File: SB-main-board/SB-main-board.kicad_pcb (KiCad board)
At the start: 4 copper layers, 53 x 40 mm, 94 parts, among them J1 XT30PB_IN, J2 USB_C_Receptacle_USB2.0_16P, J3 Excluder, J4 PT100, J5 Hotend, J6 FAN2, J7 LDC, J8 FS, J9 FAN, Q1 BUK9M8R5-40EX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

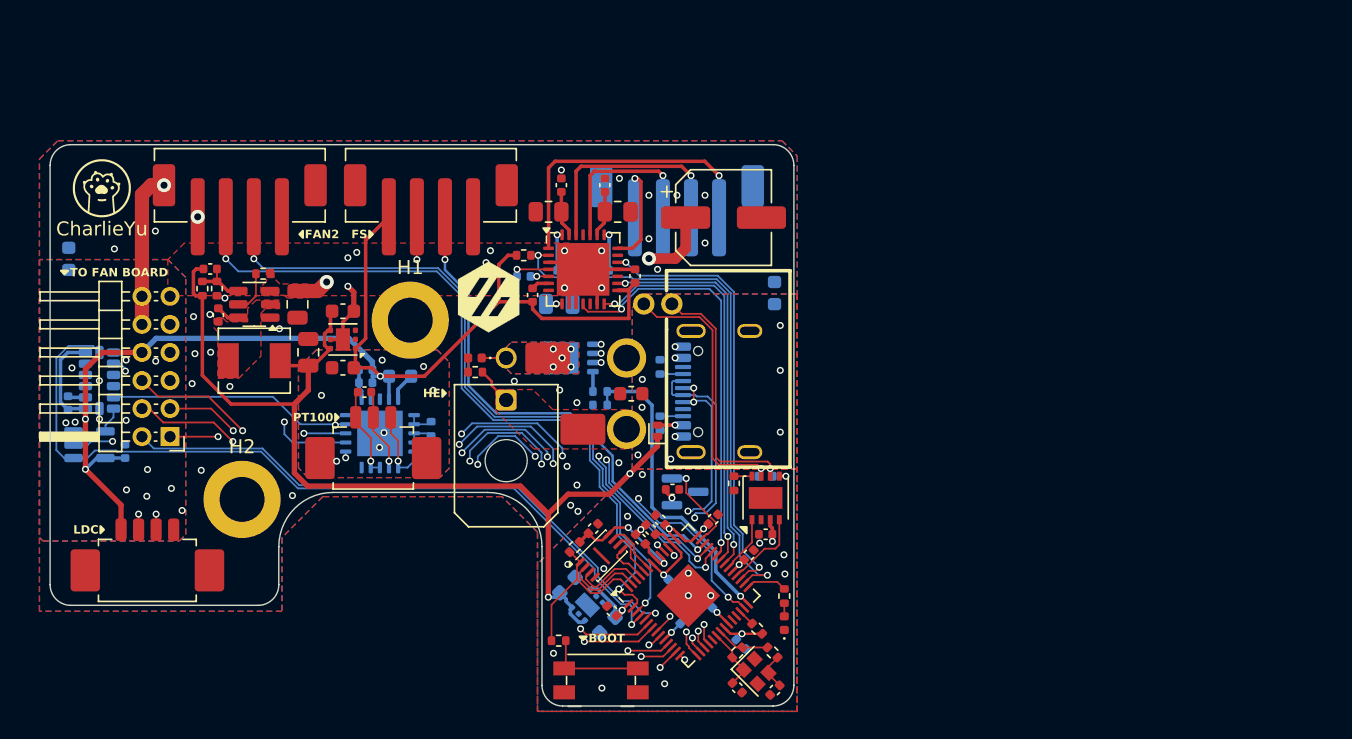
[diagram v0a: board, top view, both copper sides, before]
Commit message: mechanical: fix interference
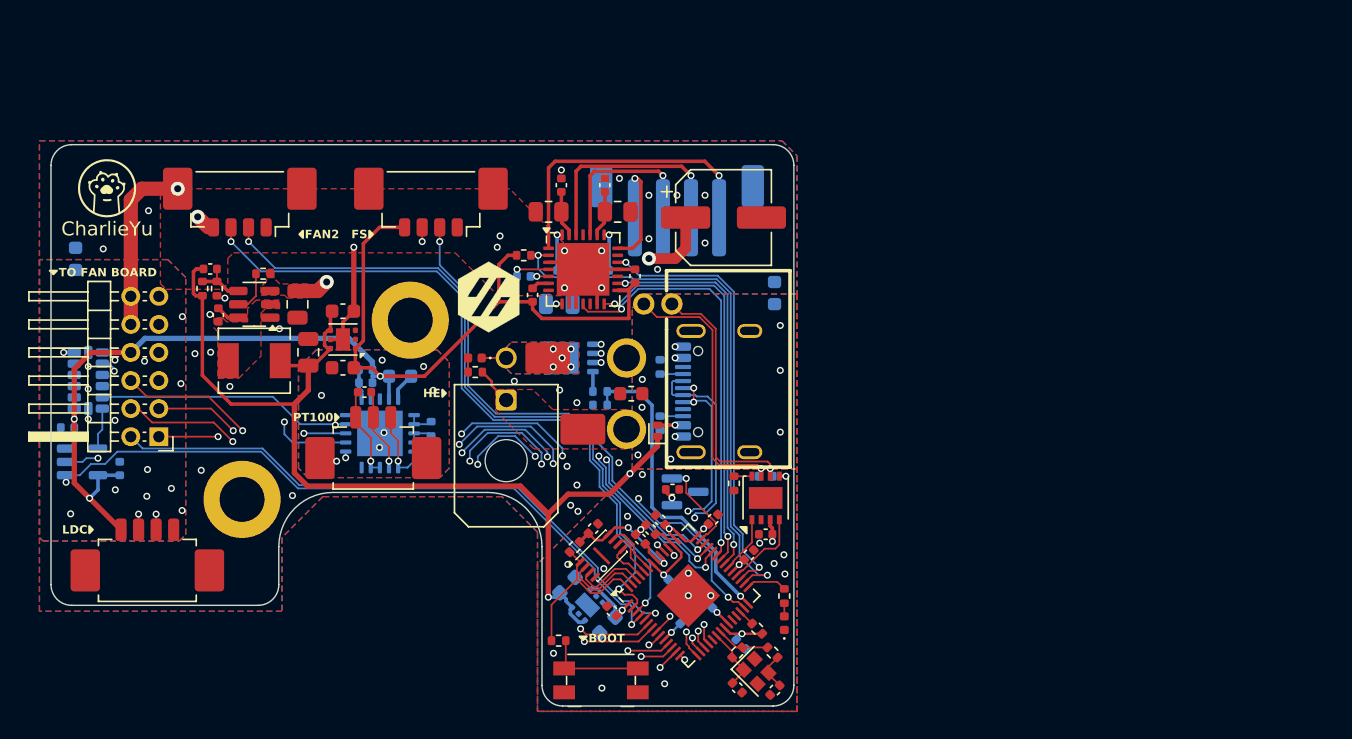
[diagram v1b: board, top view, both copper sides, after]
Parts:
- J6, J8: footprint Library:JST_PH_B4B-PH-SM4-TB_1x04-1MP_P2.00mm_Vertical -> Connector_Molex:Molex_PicoBlade_53398-0471_1x04-1MP_P1.25mm_Vertical
- moved C29 1.75 mm to (80.9, 113.8), turned to 180 degrees
- moved U7 1.34 mm to (81.9, 116.3)
- moved C30 1.28 mm to (84.6, 116.7)
- moved J9 0.80 mm to (87.4, 114.5)
- moved U8 0.80 mm to (82.3, 110.5)
- moved FB3 0.48 mm to (81.4, 101.8)
- moved RFF** 0.37 mm to (83.7, 96.8)
- turned J6 to 180 degrees
- turned J8 to 180 degrees
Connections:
- J6 pad 1: +24V -> GND
- J6 pad 2: /FAN2_PWM -> /FAN2_DET
- J6 pad 3: /FAN2_DET -> /FAN2_PWM
- J6 pad 4: GND -> +24V
- J8 pad 1: +3V3B -> GND
- J8 pad 2: /ENDSTOP0 -> /FS
- J8 pad 3: /FS -> /ENDSTOP0
- J8 pad 4: GND -> +3V3B
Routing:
- net +24V: track 72.3 -> 75.5 mm
- net /SPI0_MOSI: track 58.1 -> 59.7 mm
- net +3V3B: track 92.9 -> 94.4 mm, vias 3 -> 4
- net /FAN2_PWM: track 52.8 -> 51.3 mm
- net PGND: track 11.1 -> 12.6 mm
- net GND: track 25.3 -> 26.7 mm, vias 51 -> 47
- net Net-(U8-SDA/SDI/SDIO): track 1.86 -> 2.98 mm
- net /FAN2_DET: track 50.6 -> 49.5 mm
- net /ENDSTOP0: track 42.1 -> 41.2 mm
- net /SPI0_MISO: track 53.8 -> 54.6 mm
- net /SPI0_CLK: track 59.9 -> 60.7 mm
- net /NEO: track 43.2 -> 44.0 mm
- net /FAN1_DET: track 54.8 -> 55.6 mm
- net /FAN0_PWM: track 52.0 -> 52.8 mm
- net /FAN0_DET: track 51.3 -> 52.1 mm
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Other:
- board size 53 x 40 mm -> 52.9 x 40 mm

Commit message: mechanical: optimise installation
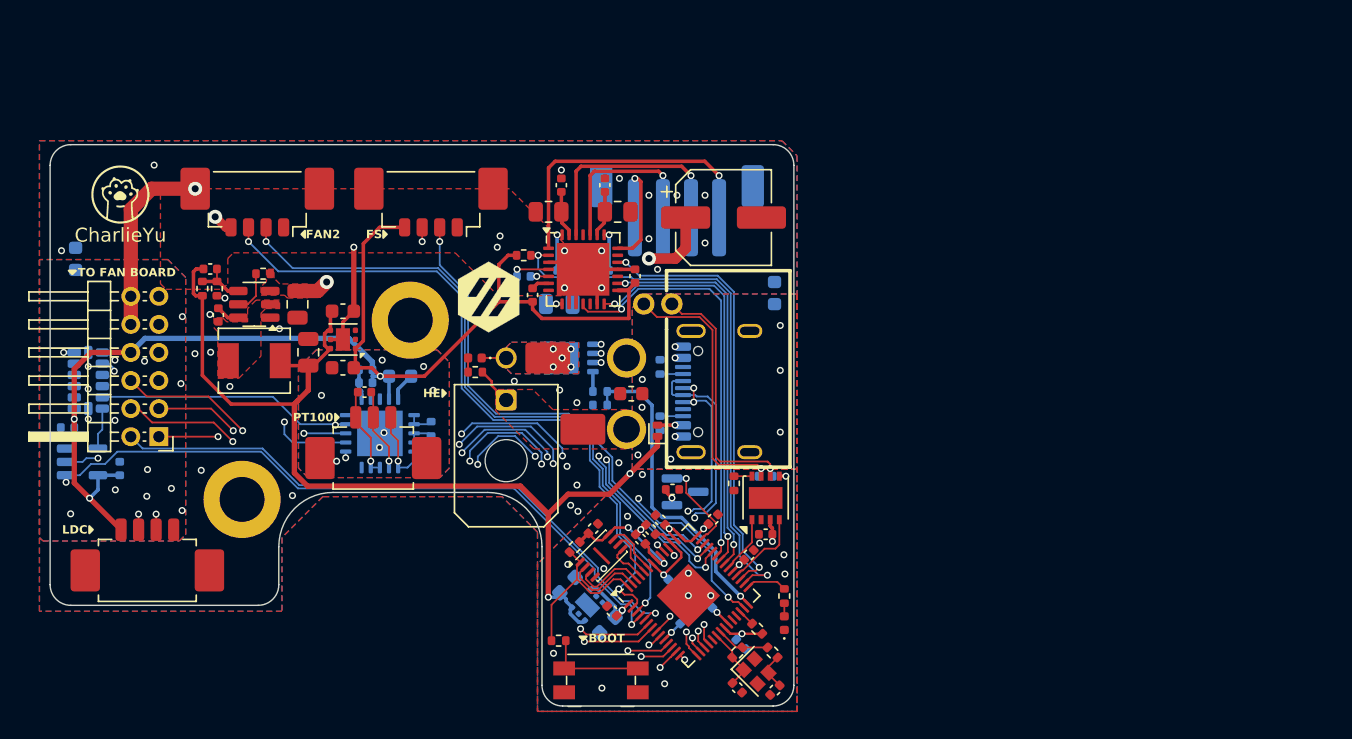
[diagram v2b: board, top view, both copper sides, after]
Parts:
- moved J6 1.25 mm to (94.4, 98.3)
- moved RFF** 1.05 mm to (84.6, 97.2)
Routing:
- net /FAN2_PWM: track 51.3 -> 49.7 mm
- net /FAN2_DET: track 49.5 -> 48.3 mm
- net PGND: track 12.6 -> 13.4 mm
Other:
- board size 52.9 x 40 mm -> 53 x 40 mm

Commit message: silkscreen: optmise silkscreen
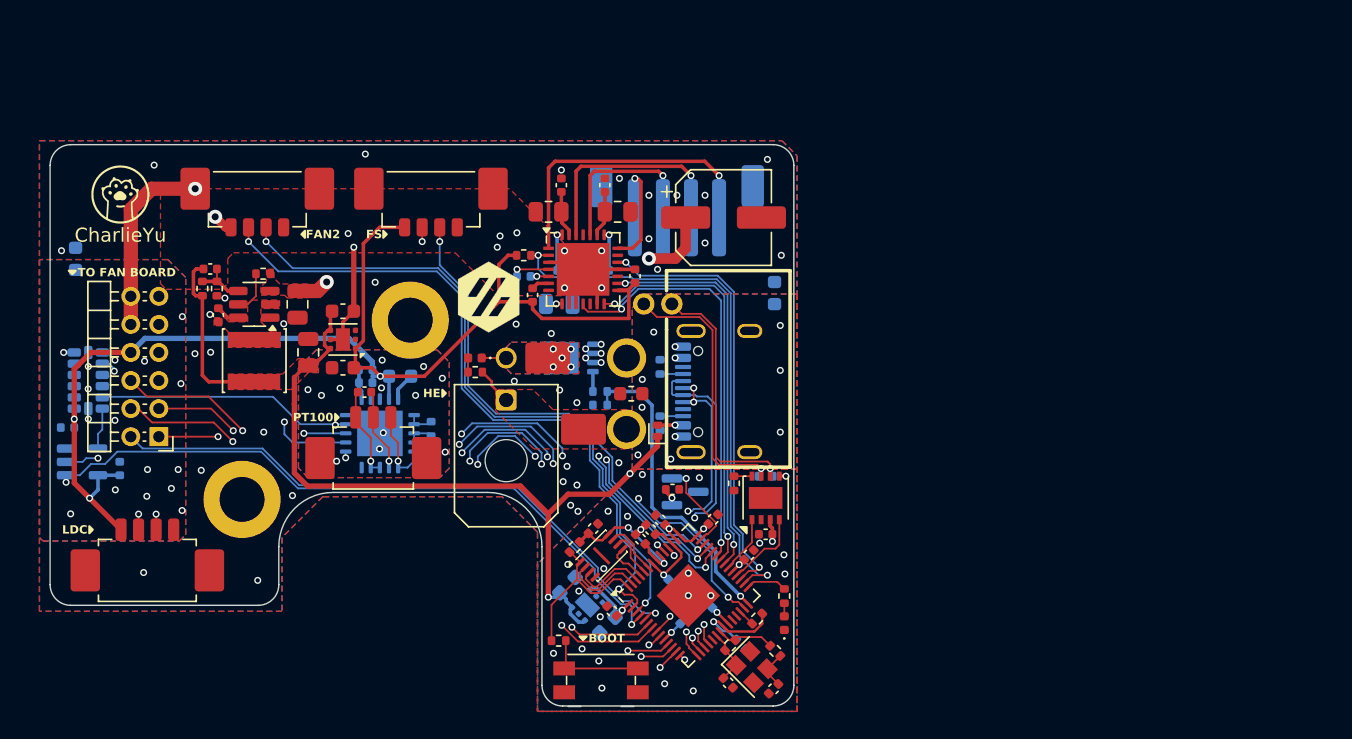
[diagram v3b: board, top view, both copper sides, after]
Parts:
- J6, J8: footprint Connector_Molex:Molex_PicoBlade_53398-0471_1x04-1MP_P1.25mm_Vertical -> Library:Molex_PicoBlade_53398-0471_1x04-1MP_P1.25mm_Vertical
- J9: footprint Connector_PinHeader_2.00mm:PinHeader_2x06_P2.00mm_Horizontal -> Library:PinHeader_2x06_P2.00mm_Horizontal
- L1: footprint Inductor_SMD:L_Chilisin_BMRA00040420 -> Inductor_SMD:L_Sunlord_SWPA4030S
- Y1: footprint Crystal:Crystal_SMD_2016-4Pin_2.0x1.6mm -> Crystal:Crystal_SMD_2520-4Pin_2.5x2.0mm
- moved C2 0.74 mm to (127.9, 132.0)
- moved R4 0.73 mm to (128.1, 129.3)
- moved R1 0.72 mm to (130.0, 127.4), turned to -135 degrees
- moved Y1 0.43 mm to (129.6, 130.9)
- moved R5 0.22 mm to (131.3, 129.7)
- moved C3 0.13 mm to (131.2, 132.4)
- turned L1 to -90 degrees
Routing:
- net +5V: track 87.1 -> 81.5 mm
- net +3V3A: track 43.4 -> 46.8 mm
- net /XIN: track 4.50 -> 3.71 mm
- net PGND: vias 32 -> 43
- net GND: vias 47 -> 63
- added copper zone on F.Cu, net +5V

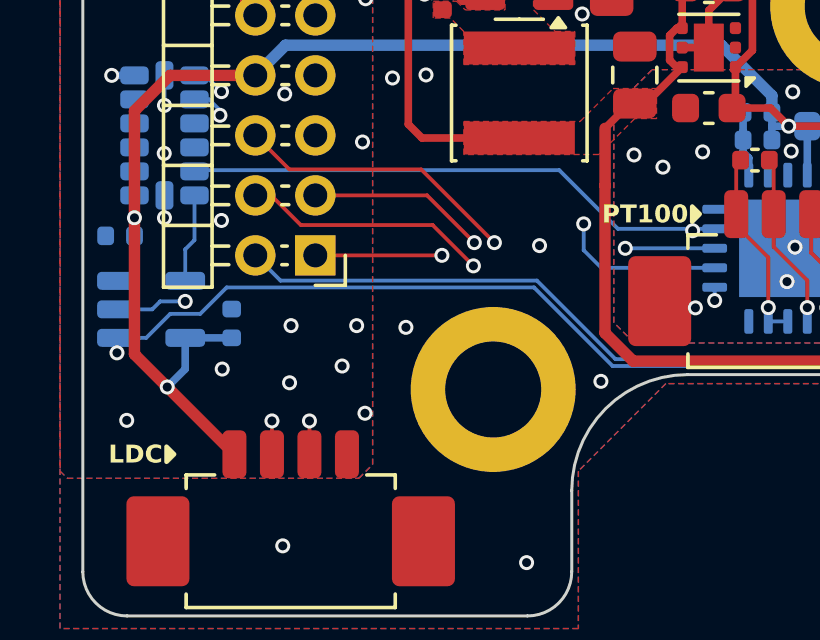
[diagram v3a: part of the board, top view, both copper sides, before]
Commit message: bugfix: use 5V for IDM sensor
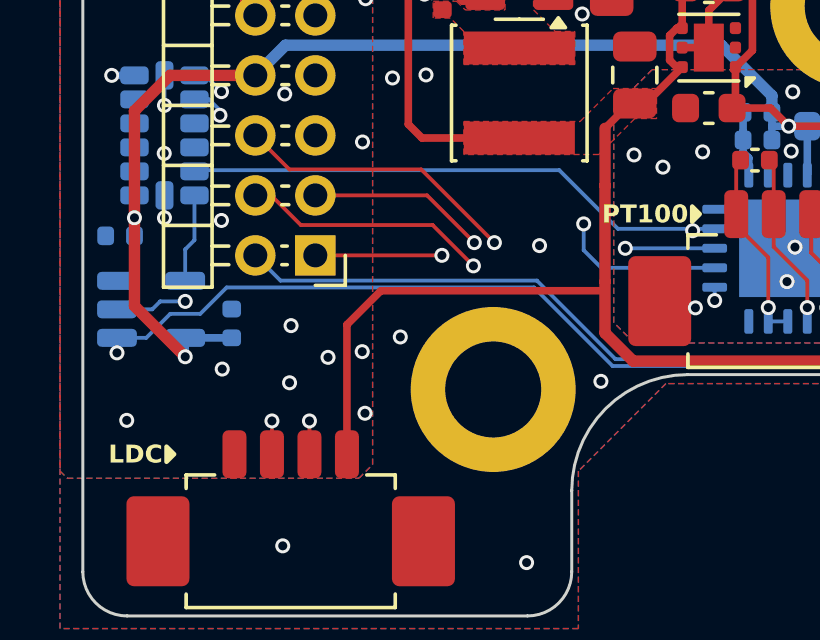
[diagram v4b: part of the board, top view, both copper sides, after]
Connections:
- J7 pad 1: +3V3B -> GND
- J7 pad 4: GND -> +5V
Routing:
- net +5V: track 81.5 -> 94.9 mm
- net +3V3B: track 94.4 -> 89.3 mm
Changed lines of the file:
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@@
 			(layers "F.Cu" "F.Paste" "F.Mask")
 			(roundrect_rratio 0.25)
-			(net 99 "+3V3B")
+			(net 2 "GND")
 			(pinfunction "Pin_1")
 			(pintype "passive")
@@
 			(layers "F.Cu" "F.Paste" "F.Mask")
 			(roundrect_rratio 0.25)
-			(net 2 "GND")
+			(net 8 "+5V")
 			(pinfunction "Pin_4")
 			(pintype "passive")
@@
 		)
 		(height 4.487268)
-		(gr_text "40.0000 mm"
+		(gr_text "1574.8031 mils"
 			(at 134.485 113.665 90)
 			(layer "F.Fab")
@@
 		)
 		(height -3.126866)
-		(gr_text "53.0000 mm"
+		(gr_text "2086.6139 mils"
 			(at 106.121594 90.862 0)
 			(layer "F.Fab")
@@
 	)
 	(via
-		(at 88.265 118.1608)
+		(at 87.795 117.872)
 		(size 0.5)
 		(drill 0.3)
@@
 	)
 	(via
-		(at 88.7496 116.8146)
+		(at 88.935 117.682)
 		(size 0.5)
 		(drill 0.3)
@@
 	)
 	(via
-		(at 90.391 116.872)
+		(at 90.205 117.192)
 		(size 0.5)
 		(drill 0.3)
@@
 	)
 	(segment
+		(start 97.028 115.352)
+		(end 97.028 117.059)
+		(width 0.381)
+		(layer "F.Cu")
+		(net 8)
+	)
+	(segment
 		(start 97.03 110.236)
 		(end 97.03 112.1488)
@@
 	)
 	(segment
+		(start 89.555 115.652)
+		(end 97.028 115.652)
+		(width 0.254)
+		(layer "F.Cu")
+		(net 8)
+	)
+	(segment
 		(start 89.835 102.722)
 		(end 89.835 104.272)
@@
 	)
 	(segment
+		(start 97.028 112.1508)
+		(end 97.028 115.352)
+		(width 0.381)
+		(layer "F.Cu")
+		(net 8)
+	)
+	(segment
 		(start 99.426 106.897)
 		(end 99.601 106.897)
@@
 	)
 	(segment
+		(start 88.426 121.102)
+		(end 88.426 116.781)
+		(width 0.254)
+		(layer "F.Cu")
+		(net 8)
+	)
+	(segment
 		(start 99.181 107.964499)
 		(end 99.181 107.142)
@@
 	)
 	(segment
+		(start 88.426 116.781)
+		(end 89.555 115.652)
+		(width 0.254)
+		(layer "F.Cu")
+		(net 8)
+	)
+	(segment
 		(start 99.601 105.6445)
 		(end 99.7135 105.532)
@@
 	)
 	(segment
-		(start 97.028 112.1508)
-		(end 97.028 117.059)
-		(width 0.381)
-		(layer "F.Cu")
-		(net 8)
-	)
-	(segment
 		(start 113.141 117.997)
 		(end 115.121866 119.977866)
@@
 	)
 	(segment
-		(start 82.435 118.861)
-		(end 84.676 121.102)
-		(width 0.381)
-		(layer "F.Cu")
-		(net 99)
-	)
-	(segment
 		(start 101.376 109.4495)
 		(end 101.2635 109.562)
@@
 	)
 	(segment
-		(start 82.435 118.861)
-		(end 81.343142 117.769142)
-		(width 0.381)
-		(layer "F.Cu")
-		(net 99)
-	)
-	(segment
 		(start 120.862392 104.120001)
 		(end 120.792392 104.050001)
@@
 	)
 	(segment
-		(start 81.343142 117.769142)
-		(end 81.343142 113.22)
-		(width 0.381)
-		(layer "F.Cu")
-		(net 99)
-	)
-	(segment
 		(start 101.376 108.197)
 		(end 101.38447 108.197)
@@
 	)
 	(segment
+		(start 83.035 117.852)
+		(end 81.343142 116.160142)
+		(width 0.381)
+		(layer "F.Cu")
+		(net 99)
+	)
+	(segment
 		(start 121.302392 103.526843)
 		(end 120.779234 104.050001)
@@
 		(net 99)
 	)
+	(segment
+		(start 81.343142 116.160142)
+		(end 81.343142 113.22)
+		(width 0.381)
+		(layer "F.Cu")
+		(net 99)
+	)
 	(via
 		(at 103.151 110.167001)
@@
 	)
 	(via
-		(at 82.435 118.861)
+		(at 83.035 117.852)
 		(size 0.5)
 		(drill 0.3)
@@
 	)
 	(segment
-		(start 82.435 118.861)
-		(end 83.035 118.261)
-		(width 0.254)
-		(layer "B.Cu")
-		(net 99)
-	)
-	(segment
 		(start 86.376742 107.4674)
 		(end 85.371142 108.473)
@@
 	)
 	(segment
-		(start 83.035 118.261)
-		(end 83.035 117.222)
+		(start 102.591 110.627001)
+		(end 102.591 110.167001)
 		(width 0.254)
 		(layer "B.Cu")
@@
 	)
 	(segment
-		(start 102.591 110.627001)
-		(end 102.591 110.167001)
+		(start 81.343142 113.22)
+		(end 81.343142 113.822)
 		(width 0.254)
 		(layer "B.Cu")
@@
 	)
 	(segment
-		(start 81.343142 113.22)
-		(end 81.343142 113.822)
+		(start 83.035 117.852)
+		(end 83.035 117.222)
 		(width 0.254)
 		(layer "B.Cu")

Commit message: fab: generate gerbers and bom
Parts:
- moved C10 38.4 mm to (167.0, 114.9)
- moved C13 38.4 mm to (160.7, 112.4)
- moved C21 38.4 mm to (158.9, 95.0)
- moved C28 38.4 mm to (153.6, 88.5)
- moved C3 38.4 mm to (168.7, 124.4)
- moved C30 38.4 mm to (122.1, 108.7)
- moved C6 38.4 mm to (160.0, 113.1)
- moved C8 38.4 mm to (166.4, 121.2)
- moved D1 38.4 mm to (169.5, 119.7)
- moved FB2 38.4 mm to (168.8, 96.2)
- moved H1 38.4 mm to (142.8, 98.1)
- moved J1 38.4 mm to (163.5, 101.6)
- moved J2 38.4 mm to (166.0, 103.2)
- moved J3 38.4 mm to (161.9, 90.3)
- moved R1 38.4 mm to (167.6, 119.4)
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
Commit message: generate gerber files
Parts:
- added S1: Select, Library:Select, B.Cu at (144.4, 108.4)
- J4: footprint Library:Molex_PicoBlade_53261-0371_1x03-1MP_P1.25mm_Horizontal -> Library:Molex_PicoBlade_53261-0471_1x04-1MP_P1.25mm_Horizontal
- R17: footprint Resistor_SMD:R_0402_1005Metric -> Resistor_SMD:R_0603_1608Metric
- moved J4 0.35 mm to (139.9, 107.5)
- moved R17 0.31 mm to (144.6, 105.9)
- moved C33 0.27 mm to (139.9, 103.3)
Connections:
- C33 pad 1: Net-(J4-Pin_2) -> Net-(J4-Pin_3)
- C33 pad 2: Net-(J4-Pin_1) -> Net-(J4-Pin_2)
- U9 pad 5: Net-(J4-Pin_3) -> Net-(J4-Pin_4)
- U9 pad 6: Net-(J4-Pin_3) -> Net-(S1-Pin_2)
- U9 pad 7: Net-(J4-Pin_2) -> Net-(J4-Pin_3)
- U9 pad 8: Net-(J4-Pin_1) -> Net-(J4-Pin_2)
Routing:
- net Net-(J4-Pin_4): track 0.00 -> 5.07 mm, vias 0 -> 1
- net Net-(S1-Pin_2): track 0.00 -> 2.54 mm
- net Net-(J4-Pin_1): track 6.96 -> 4.42 mm
- net /SPI0_MISO: track 54.6 -> 55.4 mm
- net Net-(U9-BIAS): track 1.94 -> 2.75 mm
- net Net-(U9-ISENSOR): track 1.94 -> 2.75 mm
- net /SPI0_CLK: track 60.7 -> 61.3 mm
- net +5V: track 94.9 -> 95.5 mm
- net /FAN0_PWM: track 52.8 -> 52.3 mm
- net /FAN1_PWM: track 55.1 -> 54.6 mm
- net /FAN1_DET: track 55.6 -> 55.1 mm
- net PGND: vias 43 -> 41
